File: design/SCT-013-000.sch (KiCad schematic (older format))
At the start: 2 parts, among them J1 JACK_TRS_6PINS

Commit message: Fixing connection errors
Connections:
- wire segments 9 -> 10
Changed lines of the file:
@@
 	4780 3925 5330 3925
 $Comp
-L GND #PWR033
+L GND #PWR034
 U 1 1 55B1DDA9
 P 5155 4250
-AR Path="/549598FF/55B659F5/55B1DDA9" Ref="#PWR033"  Part="1"
-AR Path="/549598FF/55B38E6D/55B1DDA9" Ref="#PWR041"  Part="1"
-AR Path="/549598FF/55B37AF3/55B1DDA9" Ref="#PWR035"  Part="1"
-AR Path="/549598FF/55B38046/55B1DDA9" Ref="#PWR037"  Part="1"
-AR Path="/549598FF/55B38E62/55B1DDA9" Ref="#PWR039"  Part="1"
-AR Path="/549598FF/55B38E78/55B1DDA9" Ref="#PWR043"  Part="1"
-F 0 "#PWR033" H 5155 4000 50  0001 C CNN
+AR Path="/549598FF/55B659F5/55B1DDA9" Ref="#PWR034"  Part="1"
+AR Path="/549598FF/55B38E6D/55B1DDA9" Ref="#PWR042"  Part="1"
+AR Path="/549598FF/55B37AF3/55B1DDA9" Ref="#PWR036"  Part="1"
+AR Path="/549598FF/55B38046/55B1DDA9" Ref="#PWR038"  Part="1"
+AR Path="/549598FF/55B38E62/55B1DDA9" Ref="#PWR040"  Part="1"
+AR Path="/549598FF/55B38E78/55B1DDA9" Ref="#PWR044"  Part="1"
+F 0 "#PWR044" H 5155 4000 50  0001 C CNN
 F 1 "GND" H 5155 4100 50  0000 C CNN
 F 2 "" H 5155 4250 60  0000 C CNN
@@
 Wire Wire Line
 	5155 3825 5330 3825
-Wire Wire Line
-	5305 4025 5155 4025
-Connection ~ 5155 4025
 $Comp
 L R R1
@@
 CT_2
 $Comp
-L +5V #PWR?
+L +5V #PWR043
 U 1 1 55B8631D
 P 4780 3025
-AR Path="/549598FF/55B38E6D/55B8631D" Ref="#PWR?"  Part="1"
-AR Path="/549598FF/55B659F5/55B8631D" Ref="#PWR?"  Part="1"
-F 0 "#PWR?" H 4780 2875 50  0001 C CNN
+AR Path="/549598FF/55B38E6D/55B8631D" Ref="#PWR043"  Part="1"
+AR Path="/549598FF/55B659F5/55B8631D" Ref="#PWR035"  Part="1"
+AR Path="/549598FF/55B37AF3/55B8631D" Ref="#PWR037"  Part="1"
+AR Path="/549598FF/55B38046/55B8631D" Ref="#PWR039"  Part="1"
+AR Path="/549598FF/55B38E62/55B8631D" Ref="#PWR041"  Part="1"
+AR Path="/549598FF/55B38E78/55B8631D" Ref="#PWR045"  Part="1"
+F 0 "#PWR045" H 4780 2875 50  0001 C CNN
 F 1 "+5V" H 4780 3165 50  0000 C CNN
 F 2 "" H 4780 3025 60  0000 C CNN
@@
 Wire Wire Line
 	4780 3075 4780 3025
+Wire Wire Line
+	5330 4025 5155 4025
+Wire Wire Line
+	5155 4025 5155 4020
+Connection ~ 5155 4020
 $EndSCHEMATC

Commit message: Agrego los dos circuitos extra para medir tension
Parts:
- J1: footprint (none) -> Pin_Headers:Pin_Header_Angled_2x03
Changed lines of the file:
@@
 LIBS:memory
 LIBS:xilinx
-LIBS:special
 LIBS:microcontrollers
 LIBS:dsp
@@
 $Descr A4 11693 8268
 encoding utf-8
-Sheet 4 18
+Sheet 5 20
 Title "PIVI"
 Date "Mon 27 Jul 2015"
@@
 AR Path="/549598FF/55B38E62/55B1DCD2" Ref="J4"  Part="1"
 AR Path="/549598FF/55B38E78/55B1DCD2" Ref="J6"  Part="1"
-F 0 "J1" H 5730 4125 50  0000 C CNN
+F 0 "J2" H 5730 4125 50  0000 C CNN
 F 1 "JACK_TRS_6PINS" H 5680 3425 50  0000 C CNN
-F 2 "" H 5830 3575 60  0001 C CNN
+F 2 "Pin_Headers:Pin_Header_Angled_2x03" H 5830 3575 60  0001 C CNN
 F 3 "" H 5830 3575 60  0000 C CNN
 	1    5730 3725
@@
 AR Path="/549598FF/55B38E62/55B1DDA9" Ref="#PWR040"  Part="1"
 AR Path="/549598FF/55B38E78/55B1DDA9" Ref="#PWR044"  Part="1"
-F 0 "#PWR044" H 5155 4000 50  0001 C CNN
+F 0 "#PWR036" H 5155 4000 50  0001 C CNN
 F 1 "GND" H 5155 4100 50  0000 C CNN
 F 2 "" H 5155 4250 60  0000 C CNN
@@
 AR Path="/549598FF/55B38E62/55B1DDFF" Ref="R4"  Part="1"
 AR Path="/549598FF/55B38E78/55B1DDFF" Ref="R16"  Part="1"
-F 0 "R1" V 4860 3225 50  0000 C CNN
+F 0 "R2" V 4860 3225 50  0000 C CNN
 F 1 "10K" V 4780 3225 50  0000 C CNN
 F 2 "Resistors_SMD:R_0603" V 4710 3225 30  0001 C CNN
@@
 AR Path="/549598FF/55B38E62/55B8631D" Ref="#PWR041"  Part="1"
 AR Path="/549598FF/55B38E78/55B8631D" Ref="#PWR045"  Part="1"
-F 0 "#PWR045" H 4780 2875 50  0001 C CNN
+F 0 "#PWR037" H 4780 2875 50  0001 C CNN
 F 1 "+5V" H 4780 3165 50  0000 C CNN
 F 2 "" H 4780 3025 60  0000 C CNN

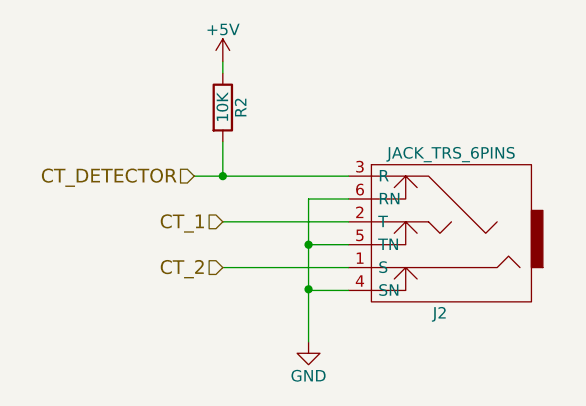
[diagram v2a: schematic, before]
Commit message: Edito conexiones pinza, agregado debub uart, agregado tension referencia
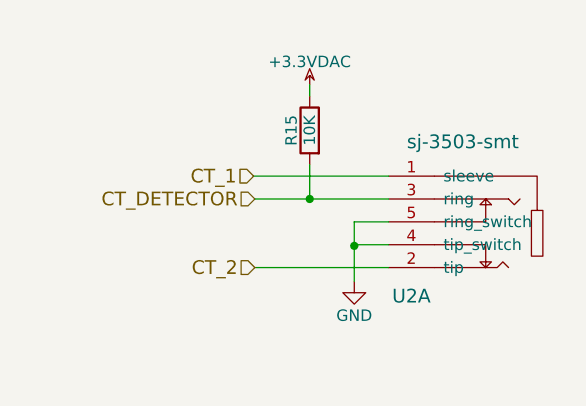
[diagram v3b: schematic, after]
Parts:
- removed J1: JACK_TRS_6PINS, Pin_Headers:Pin_Header_Angled_2x03, symbol JACK_TRS_6PINS
- added U1: sj-3503-smt, symbol sj-3503-smt
- renumbered R1 to R11
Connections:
- net CT_1: now also U1.1 (sleeve)
- net CT_2: now also U1.2 (tip)
- net CT_DETECTOR: now also U1.3 (ring)
- net GND: now also U1.4 (tip_switch), U1.5 (ring_switch)
- net +5V renamed +3.3VDAC
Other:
- moved on the sheet: R15
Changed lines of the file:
@@
 $Descr A4 11693 8268
 encoding utf-8
-Sheet 5 20
+Sheet 9 20
 Title "PIVI"
 Date "Mon 27 Jul 2015"
@@
 Comment4 ""
 $EndDescr
+Wire Wire Line
+	4920 3925 5505 3925
 $Comp
-L JACK_TRS_6PINS J1
-U 1 1 55B1DCD2
-P 5730 3725
-AR Path="/549598FF/55B659F5/55B1DCD2" Ref="J1"  Part="1"
-AR Path="/549598FF/55B38E6D/55B1DCD2" Ref="J5"  Part="1"
-AR Path="/549598FF/55B37AF3/55B1DCD2" Ref="J2"  Part="1"
-AR Path="/549598FF/55B38046/55B1DCD2" Ref="J3"  Part="1"
-AR Path="/549598FF/55B38E62/55B1DCD2" Ref="J4"  Part="1"
-AR Path="/549598FF/55B38E78/55B1DCD2" Ref="J6"  Part="1"
-F 0 "J2" H 5730 4125 50  0000 C CNN
-F 1 "JACK_TRS_6PINS" H 5680 3425 50  0000 C CNN
-F 2 "Pin_Headers:Pin_Header_Angled_2x03" H 5830 3575 60  0001 C CNN
-F 3 "" H 5830 3575 60  0000 C CNN
-	1    5730 3725
-	-1   0    0    1
+L GND #PWR35
+U 1 1 55B1DDA9
+P 5355 3985
+AR Path="/549598FF/55B37AF3/55B1DDA9" Ref="#PWR35"  Part="1"
+AR Path="/549598FF/55B659F5/55B1DDA9" Ref="#PWR33"  Part="1"
+AR Path="/549598FF/55B38046/55B1DDA9" Ref="#PWR37"  Part="1"
+AR Path="/549598FF/55B38E62/55B1DDA9" Ref="#PWR39"  Part="1"
+AR Path="/549598FF/55B38E6D/55B1DDA9" Ref="#PWR41"  Part="1"
+AR Path="/549598FF/55B38E78/55B1DDA9" Ref="#PWR43"  Part="1"
+F 0 "#PWR43" H 5355 3735 50  0001 C CNN
+F 1 "GND" H 5355 3835 50  0000 C CNN
+F 2 "" H 5355 3985 60  0000 C CNN
+F 3 "" H 5355 3985 60  0000 C CNN
+	1    5355 3985
+	1    0    0    -1
+$EndComp
+$Comp
+L R R11
+U 1 1 55B1DDFF
+P 5160 3325
+AR Path="/549598FF/55B37AF3/55B1DDFF" Ref="R11"  Part="1"
+AR Path="/549598FF/55B659F5/55B1DDFF" Ref="R10"  Part="1"
+AR Path="/549598FF/55B38046/55B1DDFF" Ref="R12"  Part="1"
+AR Path="/549598FF/55B38E62/55B1DDFF" Ref="R13"  Part="1"
+AR Path="/549598FF/55B38E6D/55B1DDFF" Ref="R14"  Part="1"
+AR Path="/549598FF/55B38E78/55B1DDFF" Ref="R15"  Part="1"
+F 0 "R15" V 5240 3325 50  0000 C CNN
+F 1 "10K" V 5160 3325 50  0000 C CNN
+F 2 "Resistors_SMD:R_0603" V 5090 3325 30  0001 C CNN
+F 3 "" H 5160 3325 30  0000 C CNN
+	1    5160 3325
+	-1   0    0    -1
 $EndComp
 Wire Wire Line
-	4780 3925 5330 3925
+	5160 3475 5160 3625
+Wire Wire Line
+	4915 3525 5505 3525
+Text HLabel 4920 3625 0    60   Input ~ 0
+CT_DETECTOR
+Text HLabel 4915 3525 0    60   Input ~ 0
+CT_1
+Text HLabel 4920 3925 0    60   Input ~ 0
+CT_2
+Wire Wire Line
+	5160 3175 5160 3125
+Wire Wire Line
+	4920 3625 5505 3625
+Connection ~ 5160 3625
+Wire Wire Line
+	5505 3825 5355 3825
+Wire Wire Line
+	5355 3825 5355 3985
+Wire Wire Line
+	5355 3830 5355 3725
+Wire Wire Line
+	5355 3725 5505 3725
+Connection ~ 5355 3830
 $Comp
-L GND #PWR034
-U 1 1 55B1DDA9
-P 5155 4250
-AR Path="/549598FF/55B659F5/55B1DDA9" Ref="#PWR034"  Part="1"
-AR Path="/549598FF/55B38E6D/55B1DDA9" Ref="#PWR042"  Part="1"
-AR Path="/549598FF/55B37AF3/55B1DDA9" Ref="#PWR036"  Part="1"
-AR Path="/549598FF/55B38046/55B1DDA9" Ref="#PWR038"  Part="1"
-AR Path="/549598FF/55B38E62/55B1DDA9" Ref="#PWR040"  Part="1"
-AR Path="/549598FF/55B38E78/55B1DDA9" Ref="#PWR044"  Part="1"
-F 0 "#PWR036" H 5155 4000 50  0001 C CNN
-F 1 "GND" H 5155 4100 50  0000 C CNN
-F 2 "" H 5155 4250 60  0000 C CNN
-F 3 "" H 5155 4250 60  0000 C CNN
-	1    5155 4250
+L +3.3VDAC #PWR34
+U 1 1 55BEA320
+P 5160 3125
+AR Path="/549598FF/55B37AF3/55BEA320" Ref="#PWR34"  Part="1"
+AR Path="/549598FF/55B659F5/55BEA320" Ref="#PWR32"  Part="1"
+AR Path="/549598FF/55B38046/55BEA320" Ref="#PWR36"  Part="1"
+AR Path="/549598FF/55B38E62/55BEA320" Ref="#PWR38"  Part="1"
+AR Path="/549598FF/55B38E6D/55BEA320" Ref="#PWR40"  Part="1"
+AR Path="/549598FF/55B38E78/55BEA320" Ref="#PWR42"  Part="1"
+F 0 "#PWR42" H 5310 3075 50  0001 C CNN
+F 1 "+3.3VDAC" H 5160 3225 50  0000 C CNN
+F 2 "" H 5160 3125 60  0000 C CNN
+F 3 "" H 5160 3125 60  0000 C CNN
+	1    5160 3125
 	1    0    0    -1
 $EndComp
-Wire Wire Line
-	5155 3625 5155 4250
-Wire Wire Line
-	5155 3825 5330 3825
 $Comp
-L R R1
-U 1 1 55B1DDFF
-P 4780 3225
-AR Path="/549598FF/55B659F5/55B1DDFF" Ref="R1"  Part="1"
-AR Path="/549598FF/55B38E6D/55B1DDFF" Ref="R5"  Part="1"
-AR Path="/549598FF/55B37AF3/55B1DDFF" Ref="R2"  Part="1"
-AR Path="/549598FF/55B38046/55B1DDFF" Ref="R3"  Part="1"
-AR Path="/549598FF/55B38E62/55B1DDFF" Ref="R4"  Part="1"
-AR Path="/549598FF/55B38E78/55B1DDFF" Ref="R16"  Part="1"
-F 0 "R2" V 4860 3225 50  0000 C CNN
-F 1 "10K" V 4780 3225 50  0000 C CNN
-F 2 "Resistors_SMD:R_0603" V 4710 3225 30  0001 C CNN
-F 3 "" H 4780 3225 30  0000 C CNN
-	1    4780 3225
+L sj-3503-smt U1
+U 1 1 55BF1B7D
+P 5680 3625
+AR Path="/549598FF/55B37AF3/55BF1B7D" Ref="U1"  Part="1"
+AR Path="/549598FF/55B659F5/55BF1B7D" Ref="U1"  Part="1"
+AR Path="/549598FF/55B38046/55BF1B7D" Ref="U1"  Part="1"
+AR Path="/549598FF/55B38E62/55BF1B7D" Ref="U1"  Part="1"
+AR Path="/549598FF/55B38E6D/55BF1B7D" Ref="U1"  Part="1"
+AR Path="/549598FF/55B38E78/55BF1B7D" Ref="U2"  Part="1"
+F 0 "U2" H 5605 3200 60  0000 C CNN
+F 1 "sj-3503-smt" H 5830 3875 60  0000 C CNN
+F 2 "" H 5680 3625 60  0000 C CNN
+F 3 "" H 5680 3625 60  0000 C CNN
+	1    5680 3625
 	1    0    0    -1
 $EndComp
-Wire Wire Line
-	4780 3375 4780 3525
-Wire Wire Line
-	4655 3525 5330 3525
-Wire Wire Line
-	4780 3725 5330 3725
-Wire Wire Line
-	5155 3625 5330 3625
-Connection ~ 5155 3825
-Text HLabel 4655 3525 0    60   Input ~ 0
-CT_DETECTOR
-Connection ~ 4780 3525
-Text HLabel 4780 3725 0    60   Input ~ 0
-CT_1
-Text HLabel 4780 3925 0    60   Input ~ 0
-CT_2
-$Comp
-L +5V #PWR043
-U 1 1 55B8631D
-P 4780 3025
-AR Path="/549598FF/55B38E6D/55B8631D" Ref="#PWR043"  Part="1"
-AR Path="/549598FF/55B659F5/55B8631D" Ref="#PWR035"  Part="1"
-AR Path="/549598FF/55B37AF3/55B8631D" Ref="#PWR037"  Part="1"
-AR Path="/549598FF/55B38046/55B8631D" Ref="#PWR039"  Part="1"
-AR Path="/549598FF/55B38E62/55B8631D" Ref="#PWR041"  Part="1"
-AR Path="/549598FF/55B38E78/55B8631D" Ref="#PWR045"  Part="1"
-F 0 "#PWR037" H 4780 2875 50  0001 C CNN
-F 1 "+5V" H 4780 3165 50  0000 C CNN
-F 2 "" H 4780 3025 60  0000 C CNN
-F 3 "" H 4780 3025 60  0000 C CNN
-	1    4780 3025
-	1    0    0    -1
-$EndComp
-Wire Wire Line
-	4780 3075 4780 3025
-Wire Wire Line
-	5330 4025 5155 4025
-Wire Wire Line
-	5155 4025 5155 4020
-Connection ~ 5155 4020
 $EndSCHEMATC
